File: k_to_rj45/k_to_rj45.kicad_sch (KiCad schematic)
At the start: 11 parts, among them J1 Conn_01x01_Female, J2 Conn_01x01_Female, J3 Conn_01x01_Female, J4 Conn_01x01_Female, J5 Conn_01x01_Female, J6 RJ45_Shielded, J7 Conn_01x01_Female, J8 Conn_01x01_Female, SW1 SW_SPDT_MSM

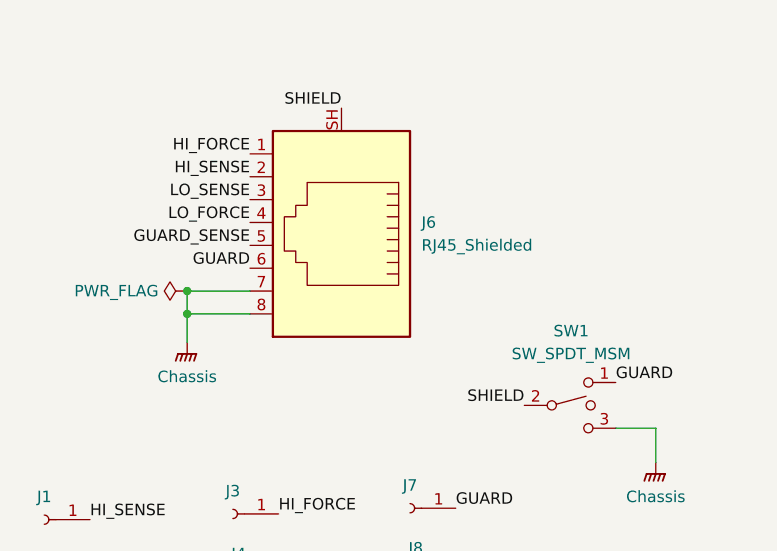
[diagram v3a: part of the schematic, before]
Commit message: fix up rj45 pad numbering
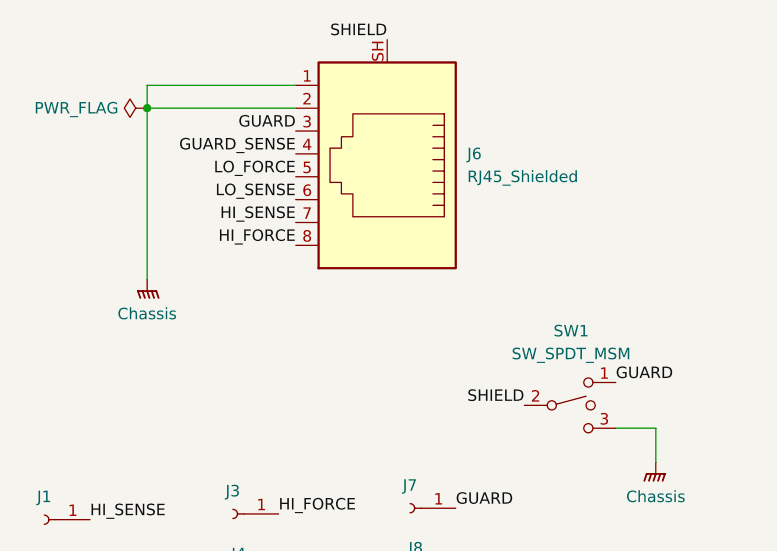
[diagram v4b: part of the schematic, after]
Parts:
- J6: footprint custom_footprints:RJ45_TE_100616-1_vertical_shield -> custom_footprints:RJ45_TE_100616
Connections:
- net GNDPWR: now also J6.1, J6.2; no longer J6.7, J6.8
- net GUARD: now also J6.3; no longer J6.6
- net GUARD_SENSE: now also J6.4; no longer J6.5
- net HI_FORCE: now also J6.8; no longer J6.1
- net HI_SENSE: now also J6.7; no longer J6.2
- net LO_FORCE: now also J6.5; no longer J6.4
- net LO_SENSE: now also J6.6; no longer J6.3
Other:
- moved on the sheet: J6
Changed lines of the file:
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@@
 (kicad_sch (version 20230121) (generator eeschema)
   (paper "A4")
-  (junction (at 131.445 86.36) (diameter 0) (color 0 0 0 0)
-  )
-  (junction (at 131.445 83.82) (diameter 0) (color 0 0 0 0)
+  (junction (at 127 63.5) (diameter 0) (color 0 0 0 0)
+  )
+  (wire (pts (xy 127 63.5) (xy 143.51 63.5))
+    (stroke (width 0) (type default))
   )
   (wire (pts (xy 142.24 121.92) (xy 146.05 121.92))
@@
     (stroke (width 0) (type default))
   )
-  (wire (pts (xy 138.43 83.82) (xy 131.445 83.82))
-    (stroke (width 0) (type default))
-  )
-  (wire (pts (xy 131.445 83.82) (xy 131.445 86.36))
-    (stroke (width 0) (type default))
-  )
   (wire (pts (xy 183.515 99.06) (xy 179.07 99.06))
     (stroke (width 0) (type default))
@@
     (stroke (width 0) (type default))
   )
-  (wire (pts (xy 138.43 86.36) (xy 131.445 86.36))
-    (stroke (width 0) (type default))
-  )
-  (wire (pts (xy 131.445 86.36) (xy 131.445 89.535))
-    (stroke (width 0) (type default))
-  )
-  (label "GUARD_SENSE" (at 138.43 78.74 180) (fields_autoplaced)
-    (effects (font (size 1.27 1.27)) (justify right bottom))
-  )
-  (label "GUARD" (at 138.43 81.28 180) (fields_autoplaced)
+  (wire (pts (xy 143.51 60.96) (xy 127 60.96))
+    (stroke (width 0) (type default))
+  )
+  (wire (pts (xy 127 63.5) (xy 127 82.55))
+    (stroke (width 0) (type default))
+  )
+  (wire (pts (xy 127 60.96) (xy 127 63.5))
+    (stroke (width 0) (type default))
+  )
+  (label "GUARD_SENSE" (at 143.51 68.58 180) (fields_autoplaced)
+    (effects (font (size 1.27 1.27)) (justify right bottom))
+  )
+  (label "GUARD" (at 143.51 66.04 180) (fields_autoplaced)
     (effects (font (size 1.27 1.27)) (justify right bottom))
   )
@@
     (effects (font (size 1.27 1.27)) (justify left bottom))
   )
-  (label "LO_SENSE" (at 138.43 73.66 180) (fields_autoplaced)
-    (effects (font (size 1.27 1.27)) (justify right bottom))
-  )
-  (label "HI_FORCE" (at 138.43 68.58 180) (fields_autoplaced)
+  (label "LO_SENSE" (at 143.51 73.66 180) (fields_autoplaced)
+    (effects (font (size 1.27 1.27)) (justify right bottom))
+  )
+  (label "HI_FORCE" (at 143.51 78.74 180) (fields_autoplaced)
     (effects (font (size 1.27 1.27)) (justify right bottom))
   )
@@
     (effects (font (size 1.27 1.27)) (justify left bottom))
   )
-  (label "HI_SENSE" (at 138.43 71.12 180) (fields_autoplaced)
+  (label "HI_SENSE" (at 143.51 76.2 180) (fields_autoplaced)
     (effects (font (size 1.27 1.27)) (justify right bottom))
   )
@@
     (effects (font (size 1.27 1.27)) (justify left bottom))
   )
-  (label "LO_FORCE" (at 138.43 76.2 180) (fields_autoplaced)
+  (label "LO_FORCE" (at 143.51 71.12 180) (fields_autoplaced)
     (effects (font (size 1.27 1.27)) (justify right bottom))
   )
@@
     (effects (font (size 1.27 1.27)) (justify left bottom))
   )
-  (label "SHIELD" (at 148.59 63.5 180) (fields_autoplaced)
+  (label "SHIELD" (at 153.67 55.88 180) (fields_autoplaced)
     (effects (font (size 1.27 1.27)) (justify right bottom))
   )
@@
     )
   )
-  (symbol (lib_id "power:PWR_FLAG") (at 131.445 83.82 90) (unit 1)
+  (symbol (lib_id "power:PWR_FLAG") (at 127 63.5 90) (mirror x) (unit 1)
     (in_bom yes) (on_board yes) (dnp no) (fields_autoplaced)
-    (property "Reference" "#FLG01" (at 129.54 83.82 0)
-      (effects (font (size 1.27 1.27)) hide)
-    )
-    (property "Value" "PWR_FLAG" (at 128.27 83.8199 90)
+    (property "Reference" "#FLG01" (at 125.095 63.5 0)
+      (effects (font (size 1.27 1.27)) hide)
+    )
+    (property "Value" "PWR_FLAG" (at 123.825 63.5001 90)
       (effects (font (size 1.27 1.27)) (justify left))
     )
-    (property "Footprint" "" (at 131.445 83.82 0)
-      (effects (font (size 1.27 1.27)) hide)
-    )
-    (property "Datasheet" "~" (at 131.445 83.82 0)
+    (property "Footprint" "" (at 127 63.5 0)
+      (effects (font (size 1.27 1.27)) hide)
+    )
+    (property "Datasheet" "~" (at 127 63.5 0)
       (effects (font (size 1.27 1.27)) hide)
     )
@@
     )
   )
-  (symbol (lib_id "Connector:RJ45_Shielded") (at 148.59 76.2 180) (unit 1)
+  (symbol (lib_id "Connector:RJ45_Shielded") (at 153.67 68.58 180) (unit 1)
     (in_bom yes) (on_board yes) (dnp no) (fields_autoplaced)
-    (property "Reference" "J6" (at 157.48 76.1999 0)
+    (property "Reference" "J6" (at 162.56 68.5799 0)
       (effects (font (size 1.27 1.27)) (justify right))
     )
-    (property "Value" "RJ45_Shielded" (at 157.48 78.7399 0)
+    (property "Value" "RJ45_Shielded" (at 162.56 71.1199 0)
       (effects (font (size 1.27 1.27)) (justify right))
     )
-    (property "Footprint" "custom_footprints:RJ45_TE_100616-1_vertical_shield" (at 148.59 76.835 90)
-      (effects (font (size 1.27 1.27)) hide)
-    )
-    (property "Datasheet" "~" (at 148.59 76.835 90)
-      (effects (font (size 1.27 1.27)) hide)
-    )
-    (property "supplier" "RS" (at 148.59 76.2 0)
-      (effects (font (size 1.27 1.27)) hide)
-    )
-    (property "supplier_partno" "782-7723" (at 148.59 76.2 0)
+    (property "Footprint" "custom_footprints:RJ45_TE_100616" (at 153.67 69.215 90)
+      (effects (font (size 1.27 1.27)) hide)
+    )
+    (property "Datasheet" "~" (at 153.67 69.215 90)
+      (effects (font (size 1.27 1.27)) hide)
+    )
+    (property "supplier" "RS" (at 153.67 68.58 0)
+      (effects (font (size 1.27 1.27)) hide)
+    )
+    (property "supplier_partno" "782-7723" (at 153.67 68.58 0)
       (effects (font (size 1.27 1.27)) hide)
     )
@@
     )
   )
-  (symbol (lib_id "power:GNDPWR") (at 131.445 89.535 0) (unit 1)
-    (in_bom yes) (on_board yes) (dnp no)
-    (property "Reference" "#PWR01" (at 131.445 94.615 0)
-      (effects (font (size 1.27 1.27)) hide)
-    )
-    (property "Value" "GNDPWR" (at 131.318 94.615 0)
-      (effects (font (size 1.27 1.27)) hide)
-    )
-    (property "Footprint" "" (at 131.445 90.805 0)
-      (effects (font (size 1.27 1.27)) hide)
-    )
-    (property "Datasheet" "" (at 131.445 90.805 0)
-      (effects (font (size 1.27 1.27)) hide)
-    )
-    (property "label" "Chassis" (at 131.445 93.345 0)
-      (effects (font (size 1.27 1.27)))
-    )
+  (symbol (lib_id "power:GNDPWR") (at 127 82.55 0) (mirror y) (unit 1)
+    (in_bom yes) (on_board yes) (dnp no)
+    (property "Reference" "#PWR01" (at 127 87.63 0)
+      (effects (font (size 1.27 1.27)) hide)
+    )
+    (property "Value" "GNDPWR" (at 127.127 87.63 0)
+      (effects (font (size 1.27 1.27)) hide)
+    )
+    (property "Footprint" "" (at 127 83.82 0)
+      (effects (font (size 1.27 1.27)) hide)
+    )
+    (property "Datasheet" "" (at 127 83.82 0)
+      (effects (font (size 1.27 1.27)) hide)
+    )
+    (property "label" "Chassis" (at 127 86.36 0)
+      (effects (font (size 1.27 1.27)))
+    )
